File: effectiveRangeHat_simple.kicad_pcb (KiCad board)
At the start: 8 copper layers, 30.6 x 66.8 mm, 124 parts, among them J1 Raspberry_Pi_2_3, J10 Conn_02x08_Odd_Even, J11 Conn_01x08, J2 BATT_CON, J3 PWR_HDR, J4 NCT_BYPASS, J5 PeriHDR, J8 I2C_EXT, P1 USB4105GFA120, Q1 2N7002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

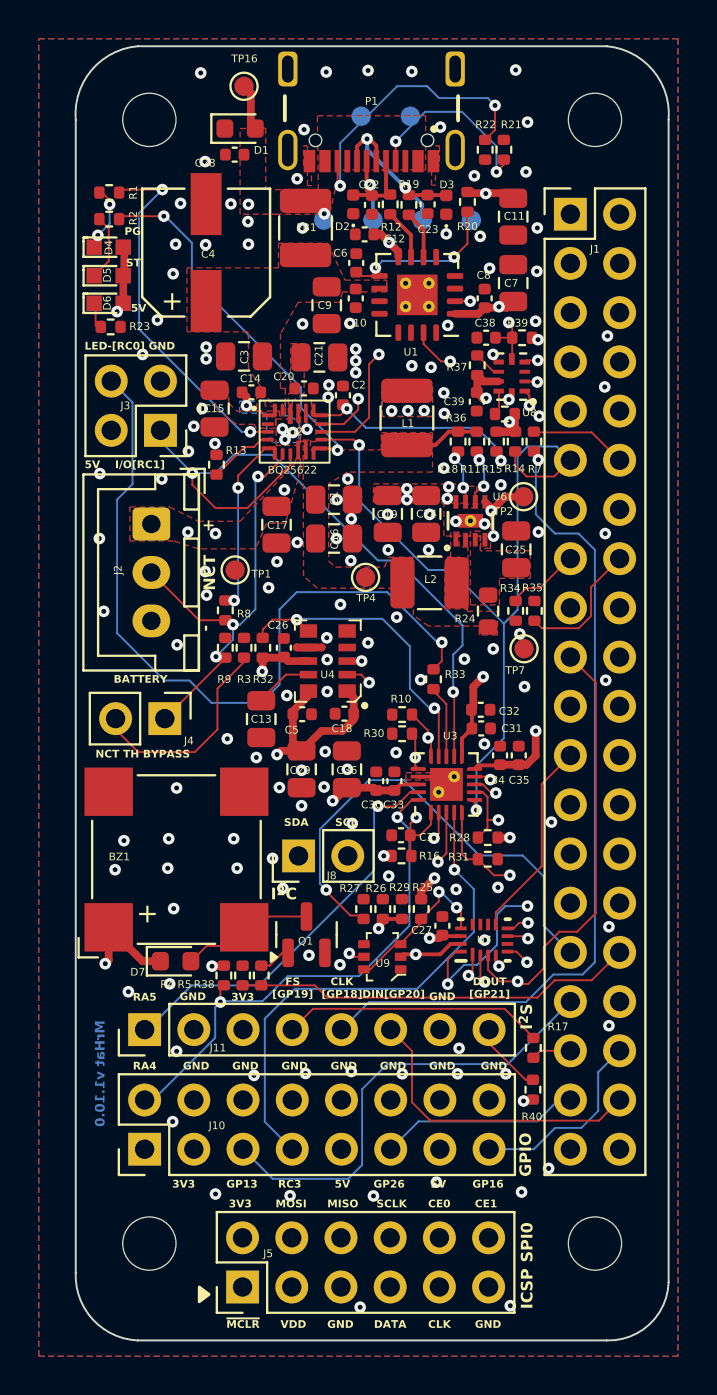
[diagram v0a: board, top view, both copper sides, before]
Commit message: fix: modifications after driver completion
- Added missing RTC IRQ to PI
- RTC VBAT is not connected to the Main Battery trough a ~1k resistor
- Connected BQ CE through a Push-pull to Open-Drain converter to PI
- Changed Mosfets to TI PicoStar model
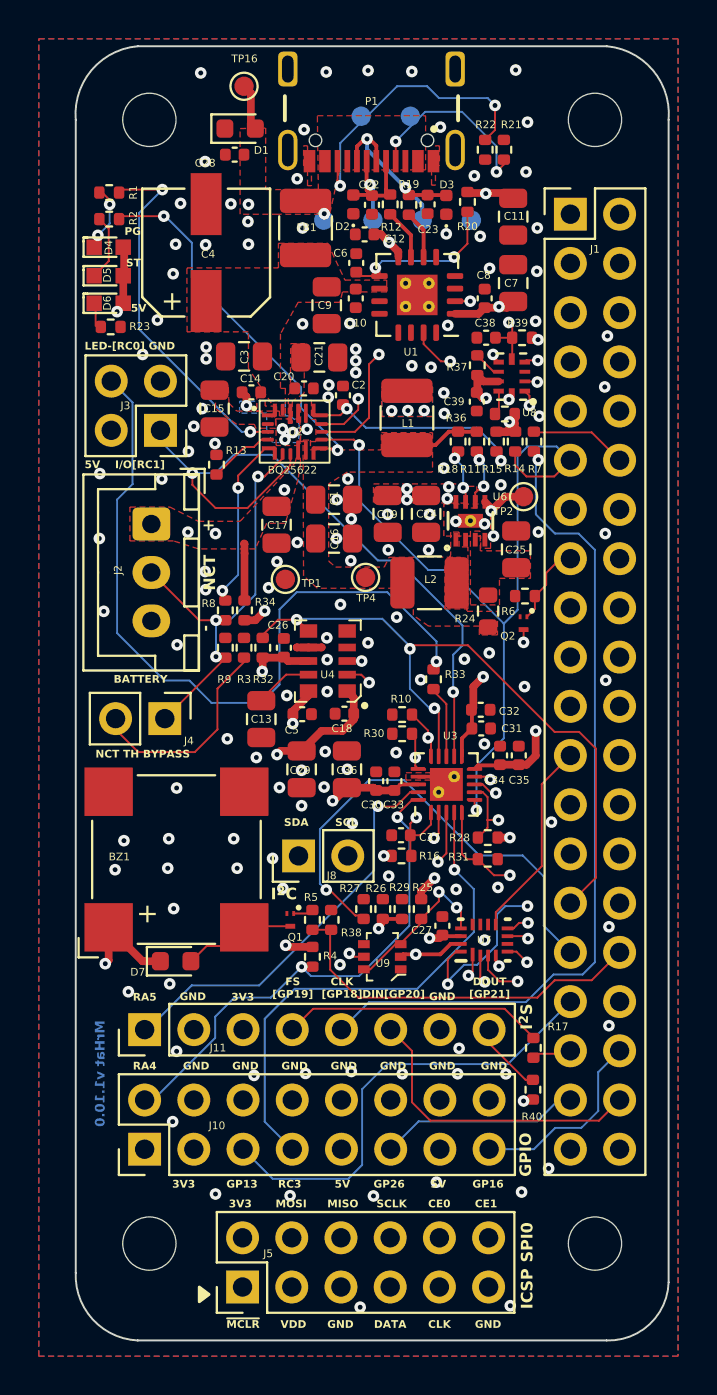
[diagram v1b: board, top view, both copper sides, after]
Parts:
- removed the G*** at (114.4, 71.5)
- removed the G*** at (128.0, 70.6)
- removed the G*** at (118.6, 71.0)
- removed R35: 1M, Resistor_SMD:R_0402_1005Metric
- removed TP7: GND, TestPoint:TestPoint_Pad_D1.0mm
- added Q2: CSD13381F4, effectiveRangeHat:YJC0003A_TEX, F.Cu at (130.0, 88.2)
- added R6: 1M, Resistor_SMD:R_0402_1005Metric, F.Cu at (130.1, 86.8)
- Q1: value 2N7002 -> CSD13381F4; footprint Package_TO_SOT_SMD:SOT-23 -> effectiveRangeHat:YJC0003A_TEX
- R34: value 1M -> 976
- moved R34 14.0 mm to (115.6, 87.5)
- moved R38 5.40 mm to (120.1, 103.5)
- moved R4 4.67 mm to (119.1, 105.4)
- moved R5 3.90 mm to (119.1, 103.5)
- moved TP1 2.64 mm to (117.7, 85.9)
- moved Q1 1.13 mm to (118.0, 103.5), turned to -90 degrees
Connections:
- C5 pad 1: +3.3V -> /ChargeEnableLogic/RTC_VBAT
- J1 pad 15: /ER_HWREV_0 -> /CE_PI
- J1 pad 16: /ER_HWREV_1 -> unconnected-(J1-GPIO23-Pad16)
- J1 pad 29: unconnected-(J1-GCLK1/GPIO5-Pad29) -> /~{RTC_IRQ}
- J1 pad 7: /~{RTC_IRQ} -> unconnected-(J1-GCLK0/GPIO4-Pad7)
- R34 pad 1: /ER_HWREV_0 -> /Power/BAT
- R34 pad 2: GND -> /ChargeEnableLogic/RTC_VBAT
- U4 pad 10: +3.3V -> /ChargeEnableLogic/RTC_VBAT
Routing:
- net /SPI_EXT.MOSI: track 64.7 -> 44.9 mm
- net /ChargeEnableLogic/RTC_VBAT: track 0.00 -> 11.1 mm, vias 0 -> 2
- net /CHG_DISA: track 37.6 -> 46.2 mm, vias 3 -> 4
- net /~{RTC_IRQ}: track 43.9 -> 36.4 mm, vias 2 -> 3
- net /ER_HWREV_1: track 6.92 -> 0.00 mm
- net /CE_PI: track 0.00 -> 4.23 mm
- net /ER_HWREV_0: track 3.80 -> 0.00 mm
- net /Power/BAT: track 0.00 -> 2.95 mm
- net +3.3V: track 38.4 -> 35.6 mm
- net /PWM0: track 20.7 -> 19.5 mm
- net /Peripheries/BUZZ_N: track 6.93 -> 5.88 mm
- net /Peripheries/Q_BASE: track 1.66 -> 1.04 mm
- net GND: vias 139 -> 137

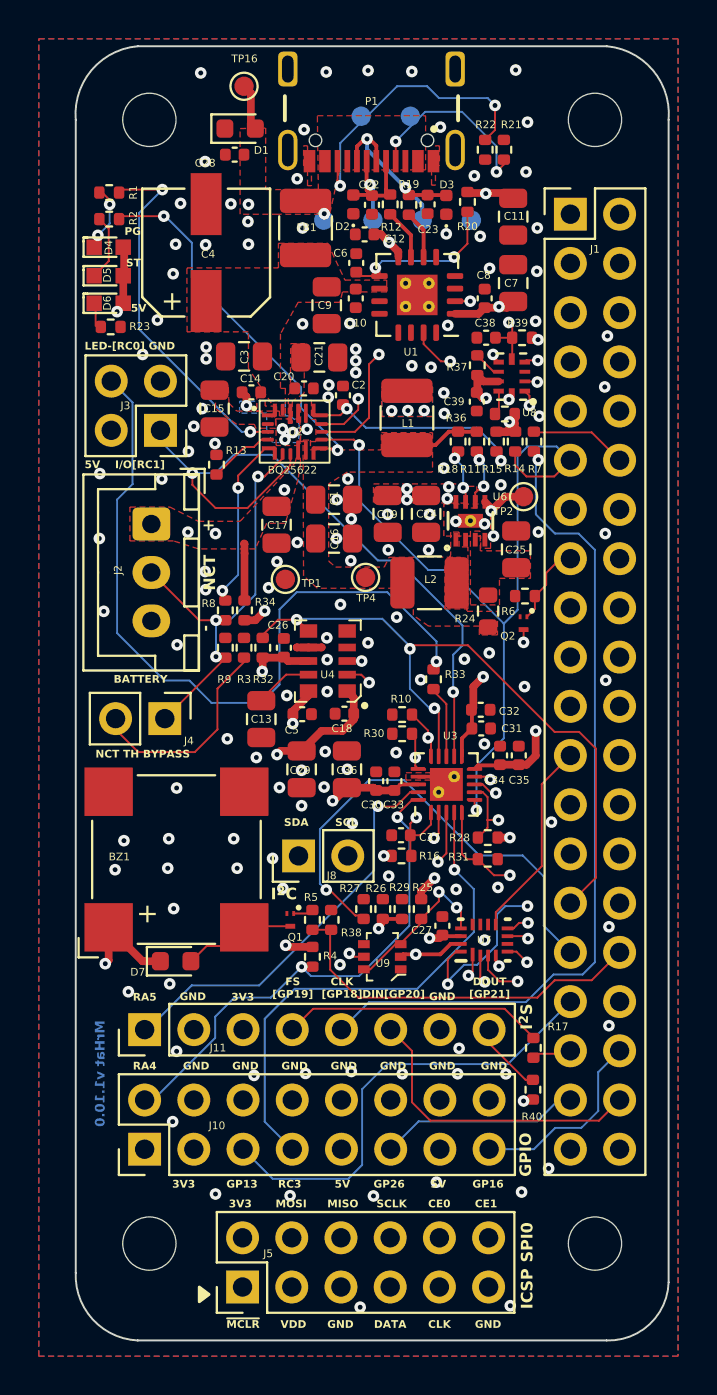
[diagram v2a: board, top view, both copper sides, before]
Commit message: fix: pcb changes, moved i2c ext header to 2x2 pin at the edge, pinout adjustments, silkscreen fixes
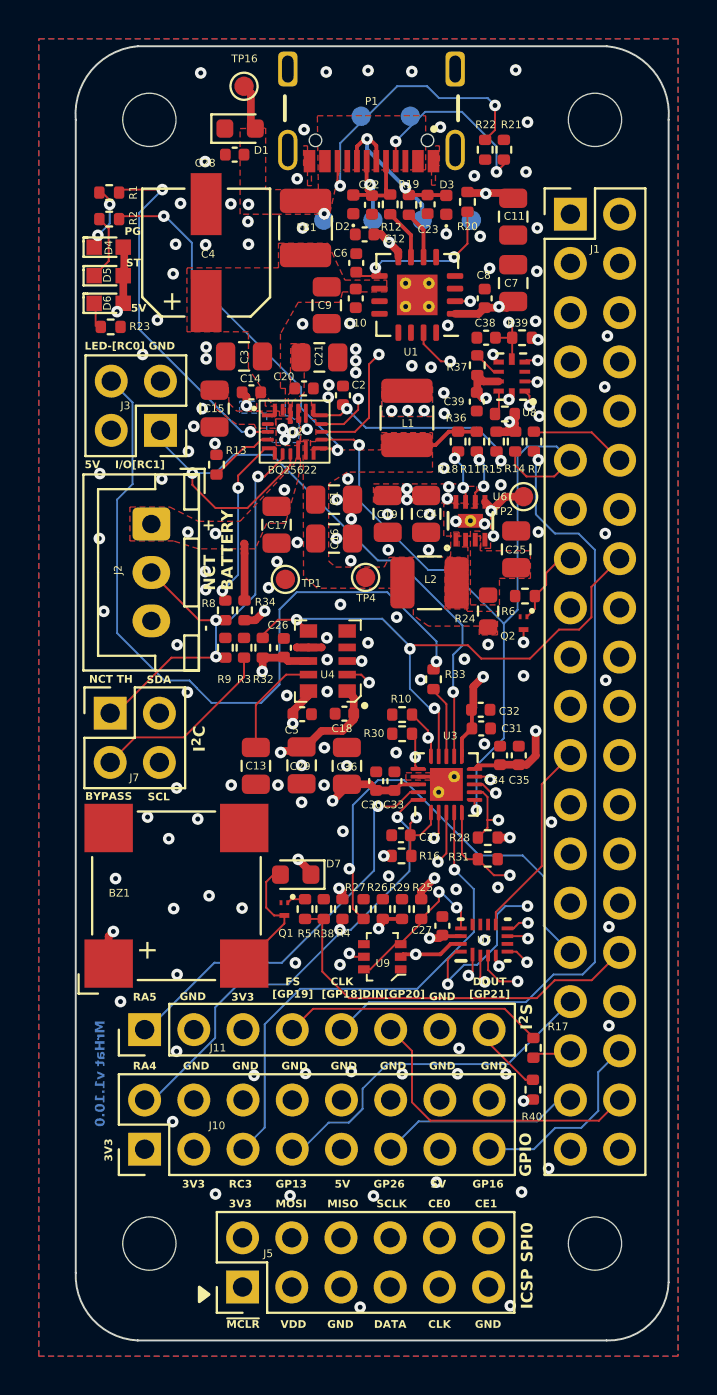
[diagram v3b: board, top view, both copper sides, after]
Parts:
- removed J4: NCT_BYPASS, Connector_PinHeader_2.54mm:PinHeader_1x02_P2.54mm_Vertical
- removed J8: I2C_EXT, Connector_PinHeader_2.54mm:PinHeader_1x02_P2.54mm_Vertical
- added J7: PWR_HDR, Connector_PinHeader_2.54mm:PinHeader_2x02_P2.54mm_Vertical, F.Cu at (108.7, 92.8)
- R34: value 976 -> 1k
- moved D7 7.64 mm to (118.3, 101.1), turned to 180 degrees
- moved R4 2.91 mm to (120.7, 102.9)
- moved C13 2.43 mm to (116.2, 95.5)
- moved BZ1 1.87 mm to (112.1, 102.2)
- moved R38 0.68 mm to (119.7, 102.9)
- moved R5 0.68 mm to (118.7, 102.9)
- moved Q1 0.64 mm to (117.7, 102.9)
- moved C29 0.20 mm to (118.6, 95.5)
- moved C36 0.18 mm to (120.9, 95.5)
- moved G*** 0.13 mm to (122.4, 89.7)
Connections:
- net /Power/TS renamed /NCT_TH_1
- J1 pad 16: unconnected-(J1-GPIO23-Pad16) -> /~{RTC_IRQ}
- J1 pad 29: /~{RTC_IRQ} -> unconnected-(J1-GCLK1/GPIO5-Pad29)
- J10 pad 5: /PWM1 -> /PIC_RC3
- J10 pad 7: /PIC_RC3 -> /PWM1
- R3 pad 1: /Power/TS_BYPASS -> /NCT_TH_2
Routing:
- net /Power/TS_BYPASS: track 11.4 -> 0.00 mm
- net /NCT_TH_2: track 0.00 -> 9.74 mm
- net /~{RTC_IRQ}: track 36.4 -> 30.2 mm
- net /PWM1: track 23.6 -> 18.1 mm
- net /SCL: track 46.3 -> 50.3 mm
- net +5V: track 25.7 -> 29.0 mm, vias 8 -> 9
- net /NCT_TH_1: track 22.6 -> 25.6 mm
- net /ChargeEnableLogic/RTC_VOUT: track 3.03 -> 5.56 mm
- net /PIC_GPIO_RA4: track 26.4 -> 24.8 mm
- net /PROG_EN: track 29.5 -> 28.3 mm
- net /PWM0: track 19.5 -> 20.6 mm
- net /SDA: track 58.6 -> 59.5 mm
- net +3.3V: track 35.6 -> 34.8 mm
- net /Peripheries/BUZZ_N: track 5.88 -> 6.67 mm
- net GND: vias 137 -> 136
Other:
- board text added: "BYPASS"
- board text added: "NCT TH"
- board text removed: "NCT TH BYPASS"
